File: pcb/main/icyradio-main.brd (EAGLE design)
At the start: 150 x 100 mm, 388 parts, among them CON301 FPC-40P, J701 TRSJACK, J702 TRSJACK, J703 TRSJACK, Q801 AO3400, Q802 AO3400, U1001 MIC23155, U1002 MIC23159, U1003 MIC2019, U1004 ADP150UJZ-1.8, U1005 ADP150UJZ-3.3, U1006 MIC94305, U1007 MIC94305, U101 EFM32GG11B420F2048GL112, U201 ATSAMV71Q21B-C, U301 ICE40HX8K-CT256, U302 SST26VF064B, U401 DSC1211DE3-C0017, U402 LTC2206, U403 R820T2, U501 ADL5385, U502 AD9117, U503 ADL5601, U601 DSC1201DE3-50M00000, U602 ADF4351, U701 TSCS25A3X1NDGXZAX, U702 CP2615, U801 ER-TFT035-6, U901 DSC1201DE3-50M00000, U902 SI5351C, X101 32.768 kHz, X401 DNP, X901 DNP

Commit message: Change FPGA_CBSEL0 signal name to FPGA_SMC_IRQ Added AD9117 library Extensively tested (lol) R820T2 library Added ARM CMSIS DSP functions to compute FFT in the SMC Small changes to the Verilog design Finally removed TFT bloat code Changed FPGA SPI from mode 3 to mode 0
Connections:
- net FPGA_CBSEL0 renamed !FPGA_SMC_IRQ
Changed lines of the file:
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@@
 <wire x1="73.28085" y1="38.48085" x2="75.9" y2="41.1" width="0.095" layer="1"/>
 </signal>
-<signal name="FPGA_CBSEL0">
+<signal name="!FPGA_SMC_IRQ">
 <contactref element="U301" pad="K11"/>
 <wire x1="68.1" y1="48.8" x2="68.500003125" y2="48.399996875" width="0.095" layer="1"/>

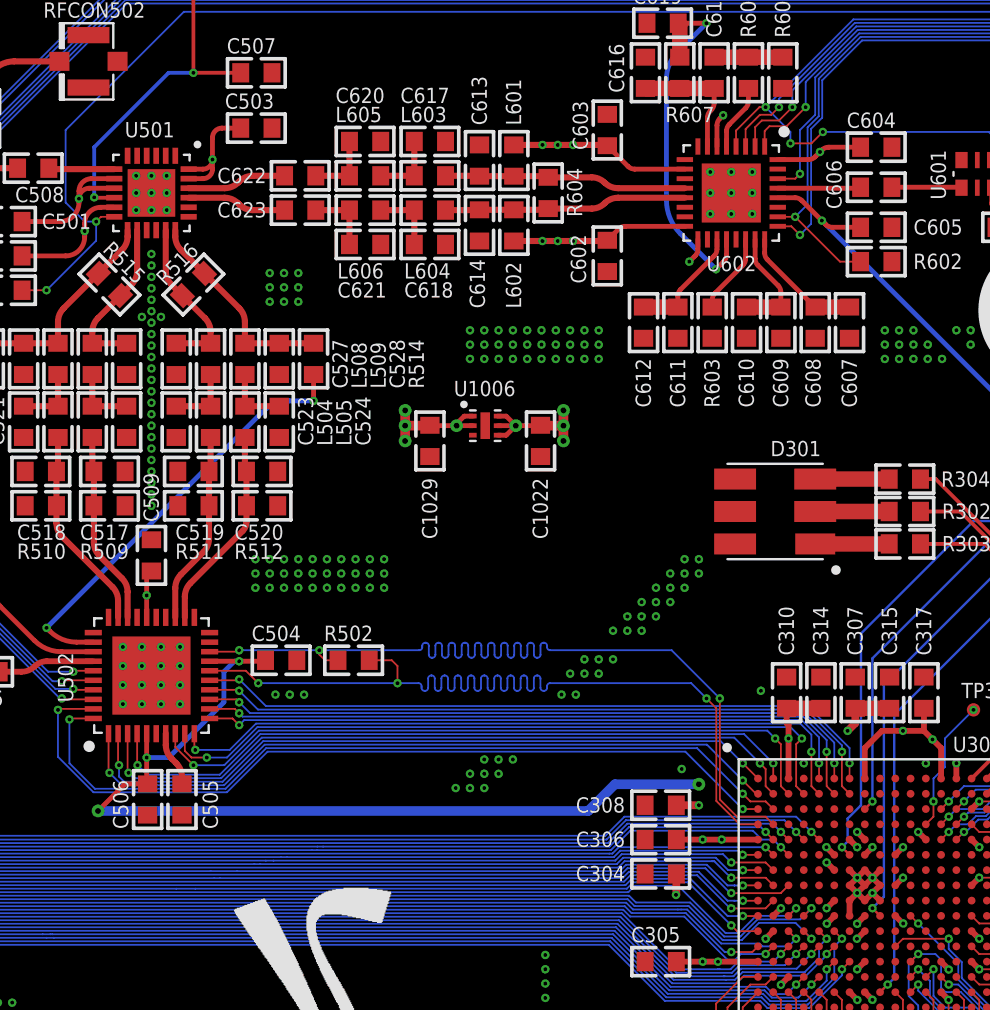
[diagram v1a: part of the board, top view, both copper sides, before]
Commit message: Tidy up HDL Add SSB modulation MATLAB script
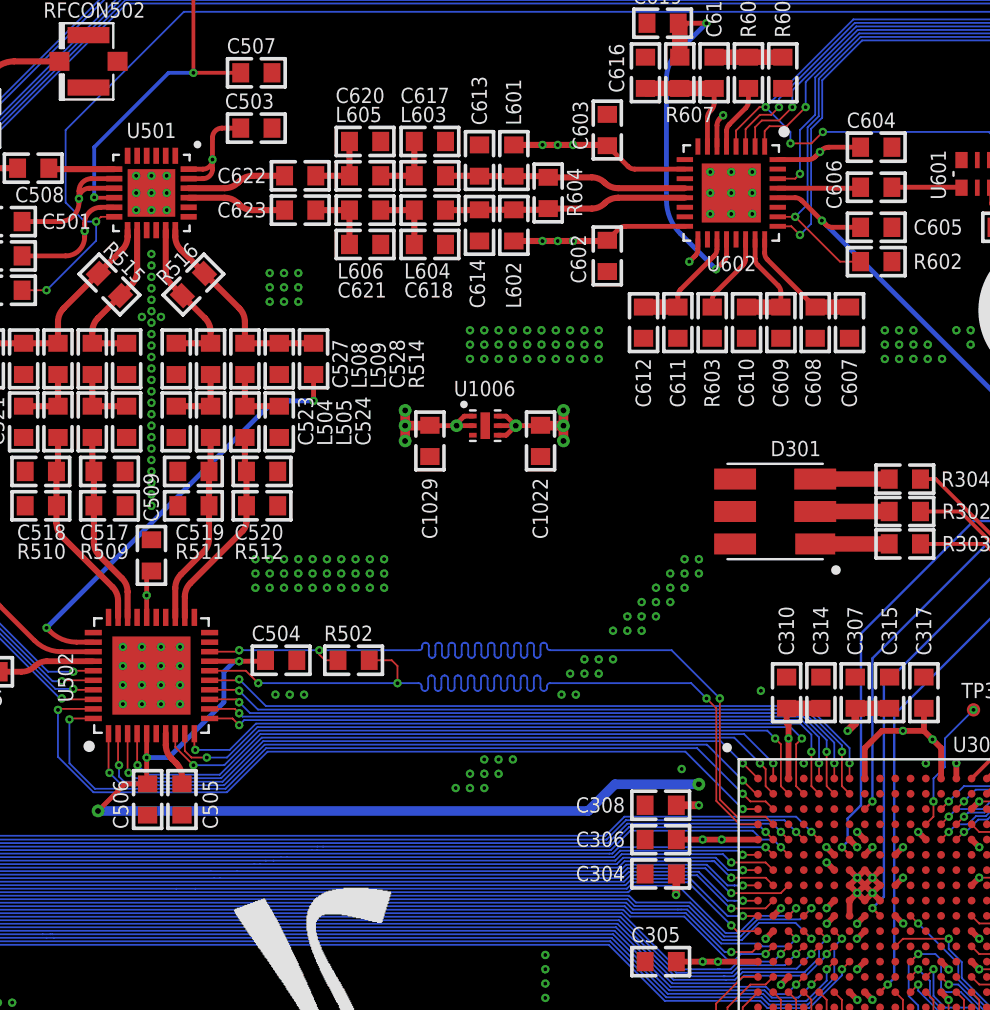
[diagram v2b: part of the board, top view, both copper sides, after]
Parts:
- turned U501 to 270 degrees
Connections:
- net GND: now also U501.25; no longer U501.33
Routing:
- net GND: track 36.6 -> 37.2 mm
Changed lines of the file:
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@@
 <?xml version="1.0" encoding="utf-8"?>
 <!DOCTYPE eagle SYSTEM "eagle.dtd">
-<eagle version="9.5.1">
+<eagle version="9.5.2">
 <drawing>
 <settings>
@@
 <attribute name="VOLTAGE" value="" x="22.1" y="88" size="1.778" layer="27" rot="R180" display="off"/>
 </element>
-<element name="U501" library="Analog Devices" package="QFN24" value="ADL5385" x="28.3" y="86.7" smashed="yes" rot="R180">
-<attribute name="NAME" x="26.9" y="90.019" size="0.8" layer="25" font="vector" ratio="10" align="center-left"/>
+<element name="U501" library="Analog Devices" package="QFN24" value="ADL5385" x="28.3" y="86.7" smashed="yes" rot="R270">
+<attribute name="NAME" x="29.6" y="89.981" size="0.8" layer="25" font="vector" ratio="10" rot="R180" align="center-left"/>
 </element>
 <element name="U1001" library="Microchip" package="DFN10" value="MIC23155" x="117.1" y="88.2" smashed="yes">
@@
 </element>
 <element name="D101" library="LED" package="0603" value="LED0603" x="110.3" y="62.5" smashed="yes" rot="R180">
-<attribute name="COLOR" value="" x="110.3" y="62.5" size="1.778" layer="27" rot="R180" display="off"/>
+<attribute name="COLOR" value="BLUE" x="110.3" y="62.5" size="1.778" layer="27" rot="R180" display="off"/>
 <attribute name="NAME" x="108.7536" y="63.916" size="0.8" layer="25" font="vector" ratio="10" rot="SR0" align="center-left"/>
 <attribute name="VALUE" x="113.2464" y="64.532" size="1.016" layer="27" ratio="10" rot="SR180"/>
@@
 </element>
 <element name="D201" library="LED" package="0603" value="LED0603" x="101.2" y="62.5" smashed="yes">
-<attribute name="COLOR" value="" x="101.2" y="62.5" size="1.778" layer="27" display="off"/>
+<attribute name="COLOR" value="WHITE" x="101.2" y="62.5" size="1.778" layer="27" display="off"/>
 <attribute name="NAME" x="99.6536" y="63.916" size="0.8" layer="25" font="vector" ratio="10" rot="SR0" align="center-left"/>
 <attribute name="VALUE" x="98.2536" y="60.468" size="1.016" layer="27" ratio="10" rot="SR0"/>
@@
 </element>
 <element name="D501" library="LED" package="0603" value="LED0603" x="11.9" y="80.1" smashed="yes">
-<attribute name="COLOR" value="" x="11.9" y="80.1" size="1.778" layer="27" display="off"/>
+<attribute name="COLOR" value="RED" x="11.9" y="80.1" size="1.778" layer="27" display="off"/>
 <attribute name="NAME" x="10.3536" y="78.716" size="0.8" layer="25" font="vector" ratio="10" rot="SR0" align="center-left"/>
 <attribute name="VALUE" x="8.9536" y="78.068" size="1.016" layer="27" ratio="10" rot="SR0"/>
@@
 </element>
 <element name="D1003" library="LED" package="0603" value="LED0603" x="145.1" y="68.8" smashed="yes">
-<attribute name="COLOR" value="" x="145.1" y="68.8" size="1.778" layer="27" display="off"/>
+<attribute name="COLOR" value="GREEN" x="145.1" y="68.8" size="1.778" layer="27" display="off"/>
 <attribute name="NAME" x="143.4536" y="67.316" size="0.8" layer="25" font="vector" ratio="10" rot="SR0" align="center-left"/>
 <attribute name="VALUE" x="142.1536" y="66.768" size="1.016" layer="27" ratio="10" rot="SR0"/>
@@
 </element>
 <element name="D1002" library="LED" package="0603" value="LED0603" x="132.4" y="94.6" smashed="yes" rot="R180">
-<attribute name="COLOR" value="" x="132.4" y="94.6" size="1.778" layer="27" rot="R180" display="off"/>
+<attribute name="COLOR" value="GREEN" x="132.4" y="94.6" size="1.778" layer="27" rot="R180" display="off"/>
 <attribute name="NAME" x="131.1536" y="96.016" size="0.8" layer="25" font="vector" ratio="10" rot="SR0" align="center-left"/>
 <attribute name="VALUE" x="135.3464" y="96.632" size="1.016" layer="27" ratio="10" rot="SR180"/>
@@
 <contactref element="C902" pad="2"/>
 <contactref element="U501" pad="4"/>
-<contactref element="U501" pad="33"/>
+<contactref element="U501" pad="25"/>
 <contactref element="U501" pad="5"/>
 <contactref element="U501" pad="6"/>
@@
 <via x="88.4" y="78.2" extent="1-16" drill="0.2"/>
 <via x="90.1" y="78" extent="1-16" drill="0.2"/>
+<wire x1="65.7" y1="50.4" x2="66.1" y2="50" width="0.3048" layer="1"/>
 </signal>
 <signal name="3V3">

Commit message: Added CP2615 code Misc software changes Sync libraries
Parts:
- turned RFCON401 to 270 degrees
- turned RFCON501 to 270 degrees
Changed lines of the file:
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@@
 <?xml version="1.0" encoding="utf-8"?>
 <!DOCTYPE eagle SYSTEM "eagle.dtd">
-<eagle version="9.5.2">
+<eagle version="9.6.1">
 <drawing>
 <settings>
@@
 <attribute name="VALUE" x="13.948" y="5.8758" size="0.8" layer="27" font="vector" ratio="10" rot="SR90" align="center-left"/>
 </element>
-<element name="RFCON401" library="RF Connector" package="SMA-EDGE" value="RFCON-SMA-EDGE" x="3.3" y="12" smashed="yes" rot="R90">
-<attribute name="NAME" x="6.07" y="16.49" size="0.8" layer="25" font="vector" ratio="10" rot="R180" align="center-left"/>
+<element name="RFCON401" library="RF Connector" package="SMA-EDGE" value="RFCON-SMA-EDGE" x="3.3" y="12" smashed="yes" rot="R270">
+<attribute name="NAME" x="0.53" y="7.51" size="0.8" layer="25" font="vector" ratio="10" align="center-left"/>
 </element>
 <element name="C420" library="Capacitor" package="CAP0603" value="1uF" x="22.9" y="7.9" smashed="yes" rot="R270">
@@
 <attribute name="VALUE" x="88.232" y="70.6456" size="0.8" layer="27" font="vector" ratio="10" rot="SR90" align="center-left"/>
 </element>
-<element name="RFCON501" library="RF Connector" package="SMA-EDGE" value="RFCON-SMA-EDGE" x="3.3" y="88" smashed="yes" rot="R90">
-<attribute name="NAME" x="5.97" y="92.49" size="0.8" layer="25" font="vector" ratio="10" rot="R180" align="center-left"/>
+<element name="RFCON501" library="RF Connector" package="SMA-EDGE" value="RFCON-SMA-EDGE" x="3.3" y="88" smashed="yes" rot="R270">
+<attribute name="NAME" x="0.63" y="83.51" size="0.8" layer="25" font="vector" ratio="10" align="center-left"/>
 </element>
 <element name="U503" library="Analog Devices" package="SOT89" value="ADL5601" x="13.6" y="86.4" smashed="yes" rot="R180">

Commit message: Remoce DAC AC swing limiting resistors Change PLL reference AC couple capacitor to 10pF
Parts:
- C606: value 100nF -> 10pF
- R515, R516: value 100 Ohms -> DNP
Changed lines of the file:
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@@
 <attribute name="VALUE" x="25.9544" y="72.332" size="0.8" layer="27" font="vector" ratio="10" rot="SR180" align="center-left"/>
 </element>
-<element name="R515" library="Resistor" package="RES0603" value="100 Ohms" x="26.1" y="81.9" smashed="yes" rot="R315">
+<element name="R515" library="Resistor" package="RES0603" value="DNP" x="26.1" y="81.9" smashed="yes" rot="R315">
 <attribute name="NAME" x="25.975790625" y="83.96105" size="0.8" layer="25" font="vector" ratio="10" rot="SR315" align="center-left"/>
 <attribute name="TOLERANCE" value="" x="26.1" y="81.9" size="1.778" layer="27" rot="R315" display="off"/>
@@
 <attribute name="VALUE" x="30.6456" y="68.268" size="0.8" layer="27" font="vector" ratio="10" rot="SR0" align="center-left"/>
 </element>
-<element name="R516" library="Resistor" package="RES0603" value="100 Ohms" x="30.5" y="81.9" smashed="yes" rot="R225">
+<element name="R516" library="Resistor" package="RES0603" value="DNP" x="30.5" y="81.9" smashed="yes" rot="R225">
 <attribute name="NAME" x="28.73895" y="82.07579375" size="0.8" layer="25" font="vector" ratio="10" rot="SR45" align="center-left"/>
 <attribute name="TOLERANCE" value="" x="30.5" y="81.9" size="1.778" layer="27" rot="R225" display="off"/>
@@
 <attribute name="VOLTAGE" value="" x="54.1" y="79.9" size="1.778" layer="27" rot="R270" display="off"/>
 </element>
-<element name="C606" library="Capacitor" package="CAP0603" value="100nF" x="66.3" y="87" smashed="yes" rot="R180">
+<element name="C606" library="Capacitor" package="CAP0603" value="10pF" x="66.3" y="87" smashed="yes" rot="R180">
 <attribute name="NAME" x="64.084" y="85.8536" size="0.8" layer="25" font="vector" ratio="10" rot="SR90" align="center-left"/>
 <attribute name="VALUE" x="69.2464" y="89.032" size="0.8" layer="27" font="vector" ratio="10" rot="SR180" align="center-left"/>

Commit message: Change final amplifier to ADL5610
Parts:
- U503: value ADL5601 -> ADL5610
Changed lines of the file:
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@@
 <attribute name="NAME" x="0.63" y="83.51" size="0.8" layer="25" font="vector" ratio="10" align="center-left"/>
 </element>
-<element name="U503" library="Analog Devices" package="SOT89" value="ADL5601" x="13.6" y="86.4" smashed="yes" rot="R180">
+<element name="U503" library="Analog Devices" package="SOT89" value="ADL5610" x="13.6" y="86.4" smashed="yes" rot="R180">
 <attribute name="NAME" x="14.93" y="84.44" size="0.8" layer="25" font="vector" ratio="10" align="center-left"/>
 </element>
